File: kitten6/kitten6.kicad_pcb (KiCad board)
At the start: 2 copper layers, 92.1 x 60.3 mm, 10 parts, among them SW1 SW_Push, SW2 SW_Push, SW3 SW_Push, SW4 SW_Push, SW5 SW_Push, SW6 SW_Push, SW7 SW_Push, SW8 SW_Push, U1 Pico

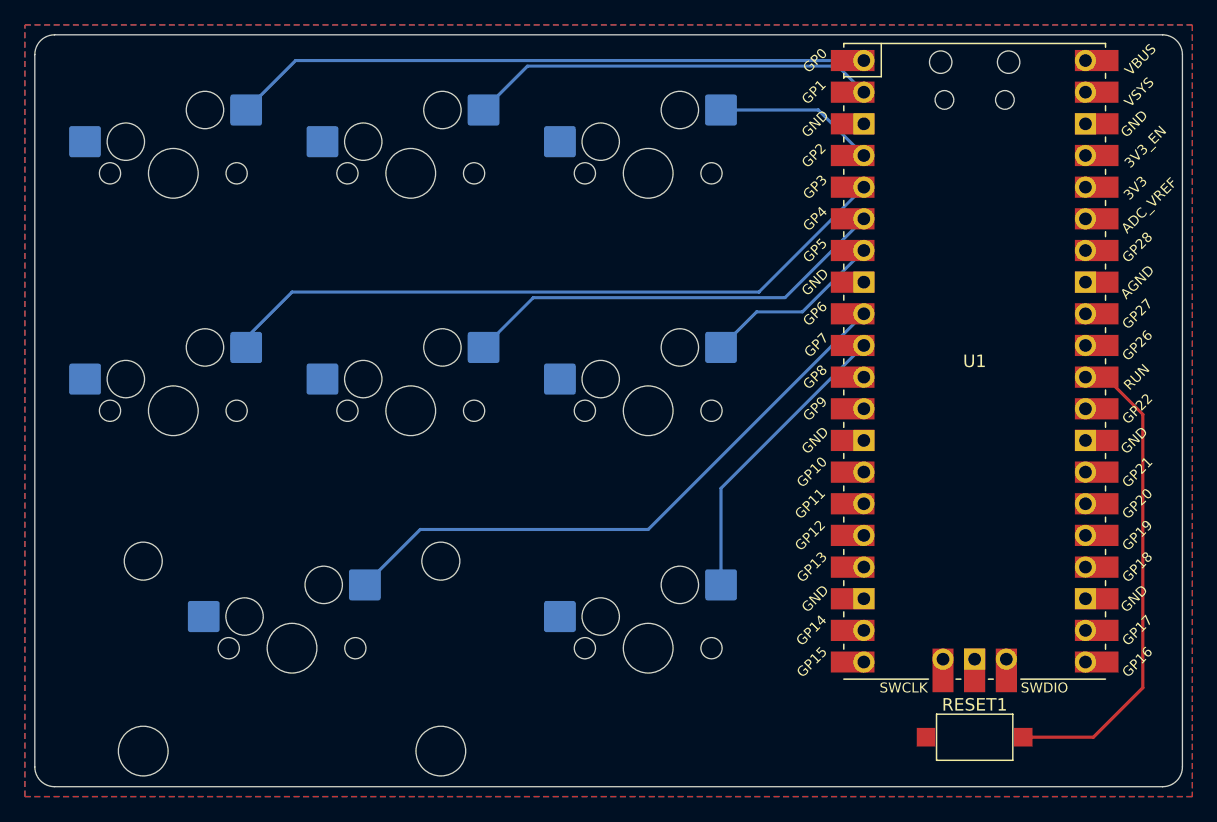
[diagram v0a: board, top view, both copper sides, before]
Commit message: Change keypad layout
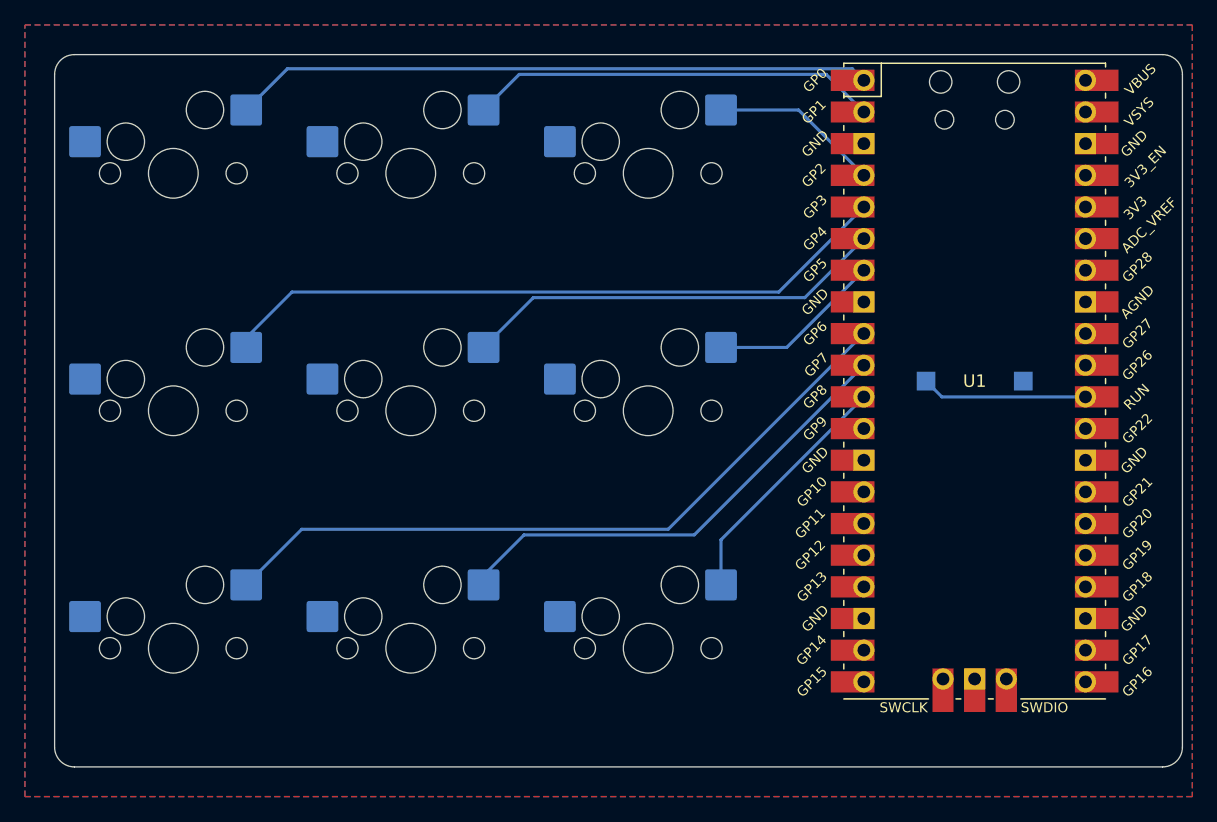
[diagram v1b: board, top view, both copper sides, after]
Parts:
- added SW9: SW_Push, MX_Hotswap:MX-Hotswap-1U, F.Cu at (164.3, 105.6)
- RESET1: moved to B.Cu
- SW7: footprint MX_Hotswap:MX-Hotswap-2U -> MX_Hotswap:MX-Hotswap-1U
- moved RESET1 28.6 mm to (190.5, 84.1), turned to 180 degrees
- moved SW8 19.1 mm to (145.3, 105.6)
- moved SW7 9.52 mm to (126.2, 105.6)
- moved U1 1.59 mm to (190.5, 84.1)
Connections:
- U1 pad 11: unconnected-(U1-Pad11) -> sw8
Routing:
- net reset: track 39.0 -> 13.3 mm
- net sw8: track 0.00 -> 19.8 mm
- net sw7: track 24.0 -> 38.3 mm
- net sw6: track 49.0 -> 57.9 mm
- net sw5: track 14.7 -> 14.0 mm
- net sw3: track 55.3 -> 54.7 mm
- net sw2: track 13.0 -> 13.6 mm
- net sw4: track 34.8 -> 34.1 mm
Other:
- board size 92.1 x 60.3 mm -> 90.5 x 57.1 mm
